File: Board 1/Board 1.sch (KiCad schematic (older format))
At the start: 85 parts, among them J10 NEG. NULL, J18 POS. NULL, J2 Y INPUT, J3 X INPUT, J5 OUTPUT, J6 +15V, J7 GND, J8 -15V, J9 GAIN TRIM, T1 TIP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

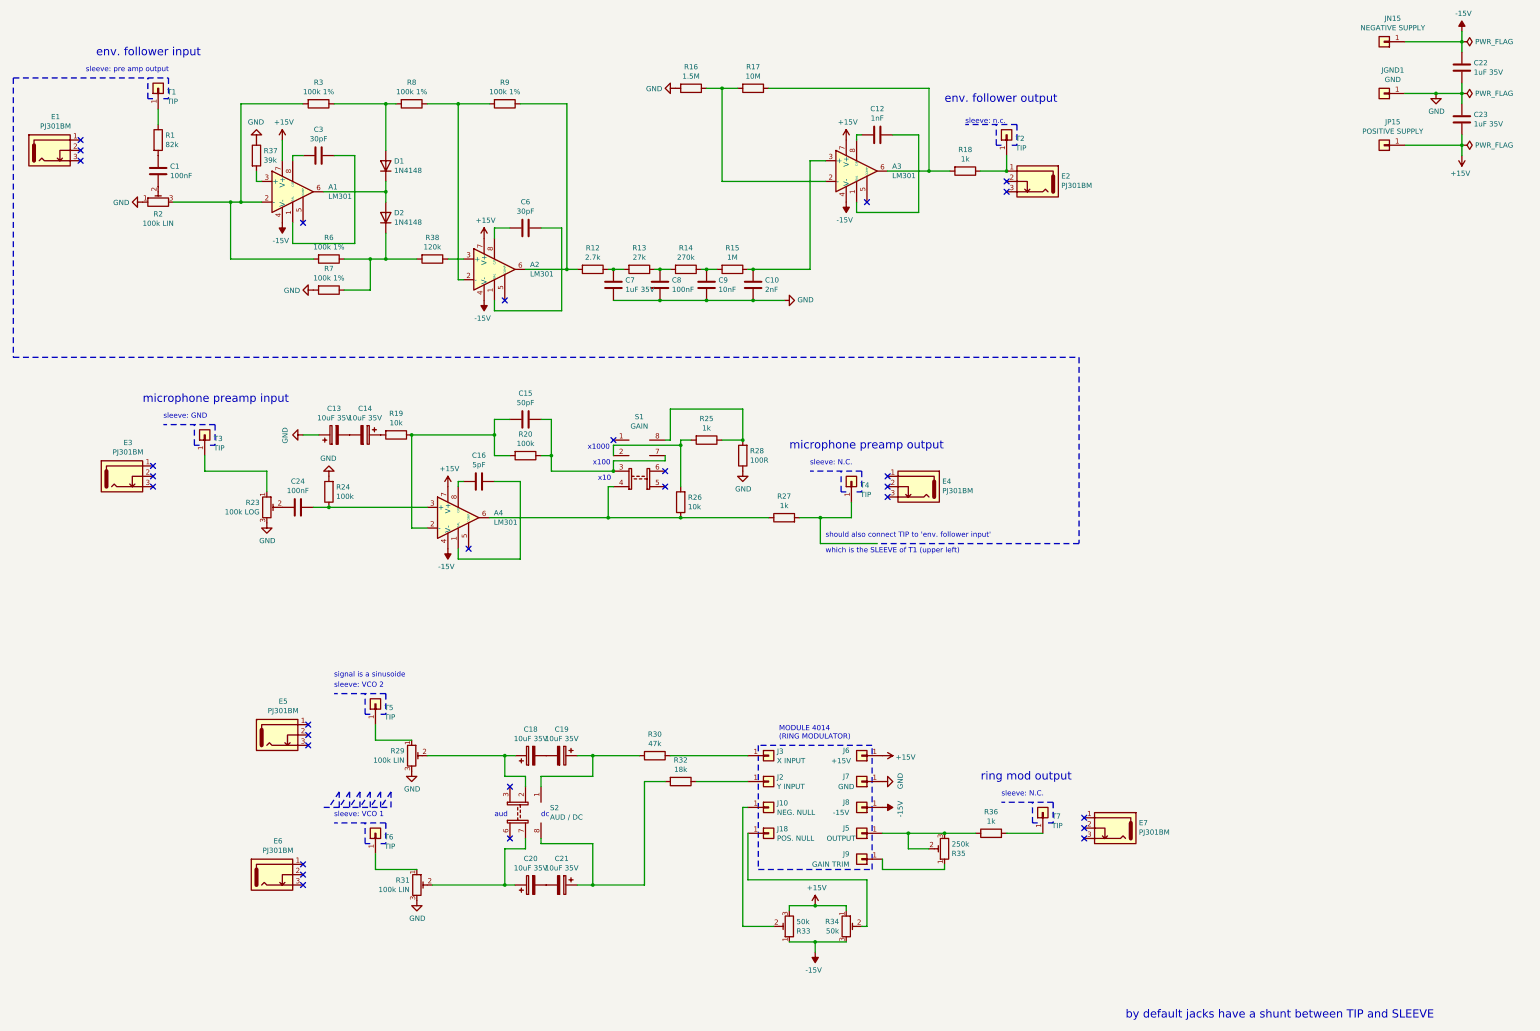
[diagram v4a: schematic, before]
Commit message: fixes for the jack connectors
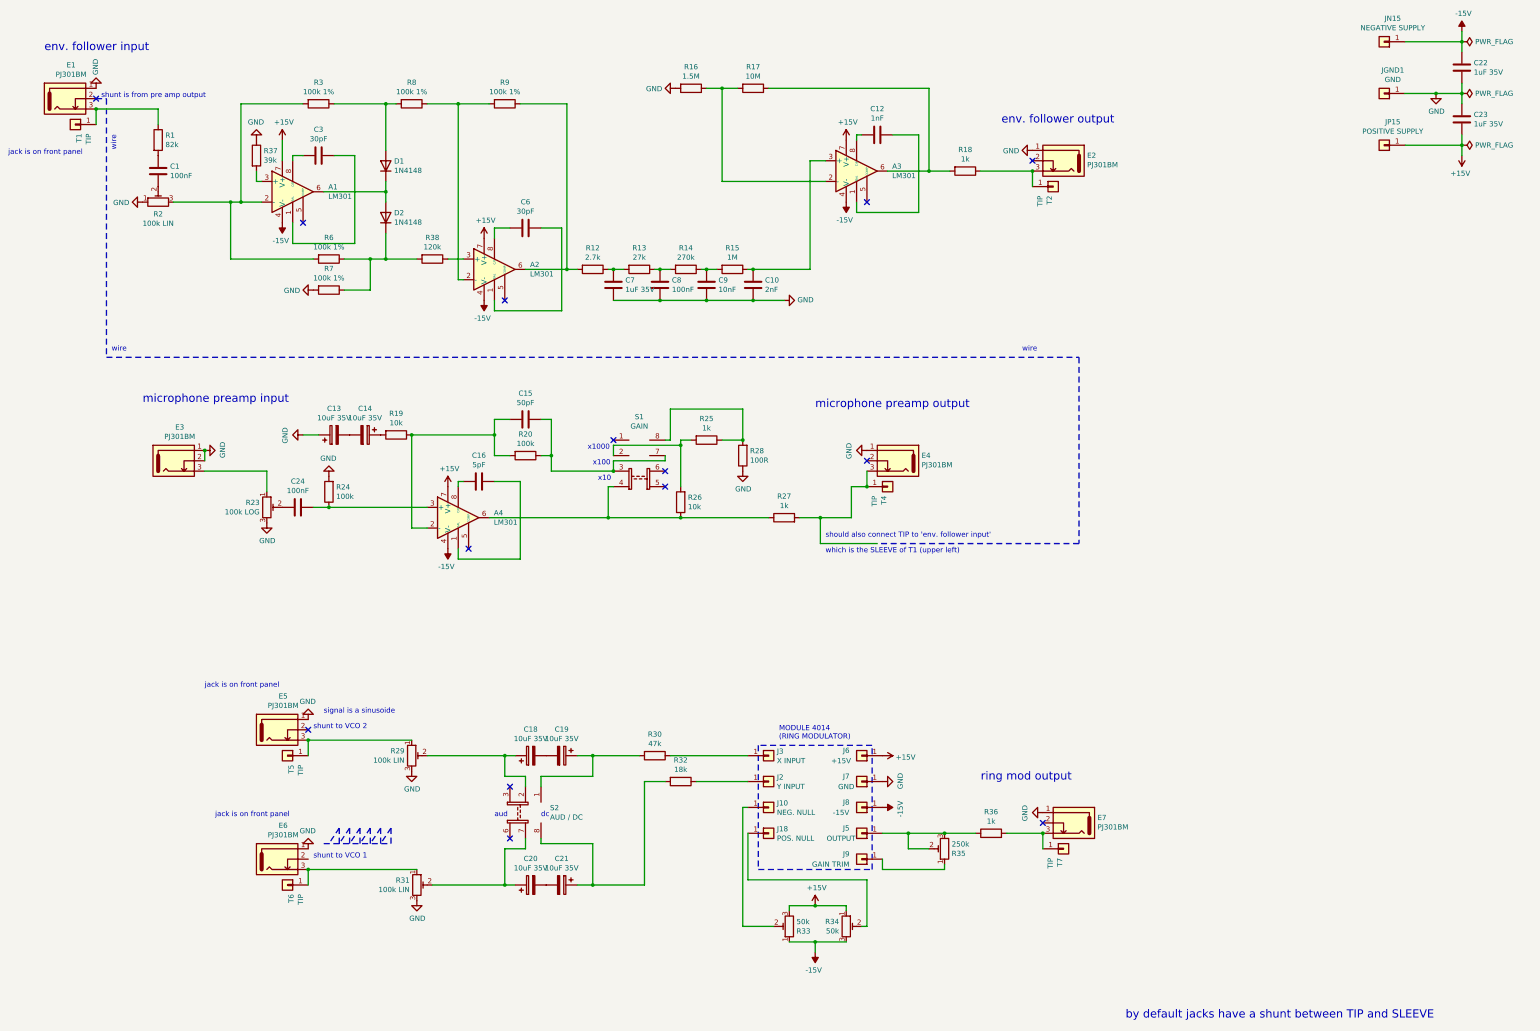
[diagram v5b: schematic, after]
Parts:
- removed T3: TIP, symbol Connector_Generic:Conn_01x01
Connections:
- net GND: now also E1.1, E2.1, E3.1, E3.2, E4.1, E5.1, E6.1, E7.1
- net at E1.3: now also R1.1, T1.1 (Pin_1)
- net at R18.1, T2.1 (Pin_1): now also E2.3; no longer E2.1
- net at E4.3: now also R27.2, T4.1 (Pin_1)
- net at E3.3: now also R23.1
- net at E5.3: now also R29.1, T5.1 (Pin_1)
- net at E6.3: now also R31.1, T6.1 (Pin_1)
- net at E7.3: now also R36.2, T7.1 (Pin_1)
- no-connect marks 29 -> 14
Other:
- note added: "jack is on front panel"
- note added: "shunt is from pre amp output"
- note added: "shunt to VCO 1"
- note added: "shunt to VCO 2"
- note added: "wire"
- note removed: "sleeve: GND"
- note removed: "sleeve: N.C."
- note removed: "sleeve: VCO 1"
- note removed: "sleeve: VCO 2"
- note removed: "sleeve: n.c."
- note removed: "sleeve: pre amp output"
- moved on the sheet: E1, E2, E3, E4, E5, E6, E7, T1, T2, T4, T5, T6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
